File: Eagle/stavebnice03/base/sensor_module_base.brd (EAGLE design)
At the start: 21 x 21 mm, 19 parts

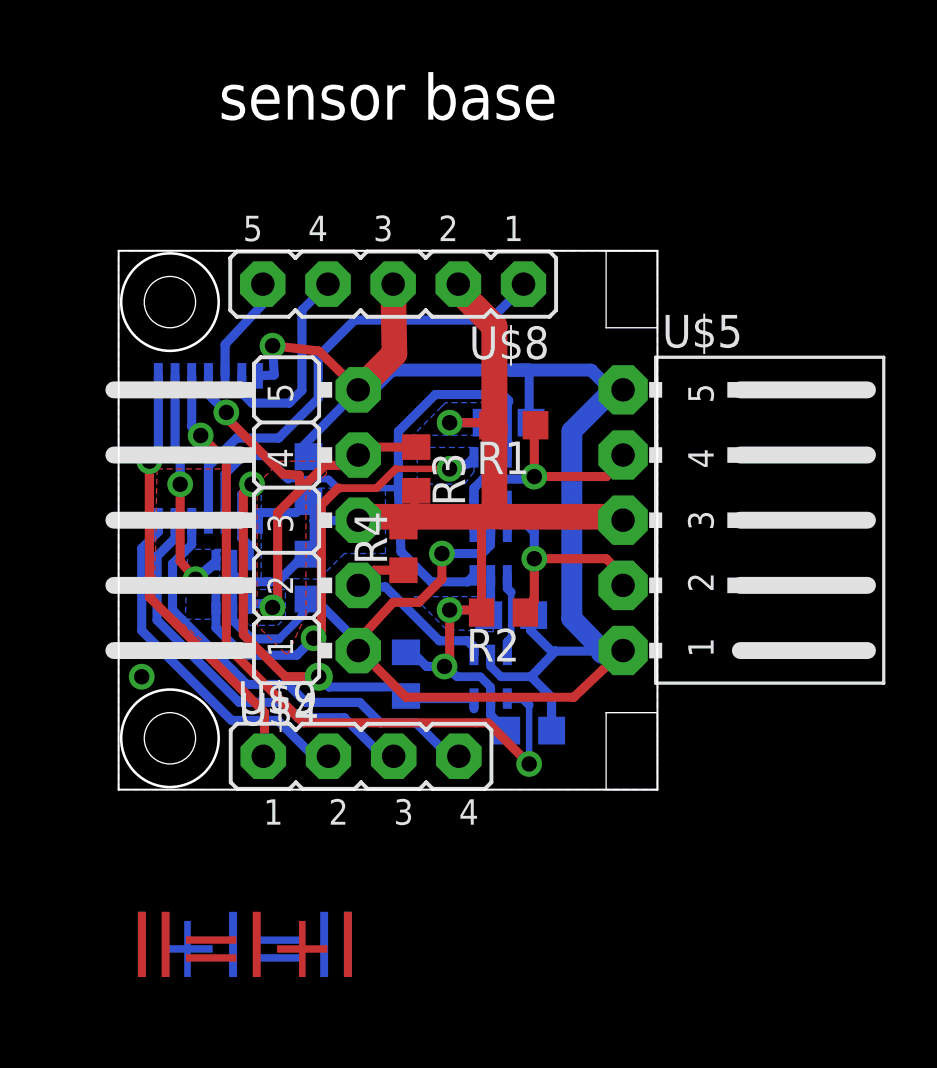
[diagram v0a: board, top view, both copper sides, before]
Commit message: layer coloring and place drawing moved to docu layer + changed sizes of names and values
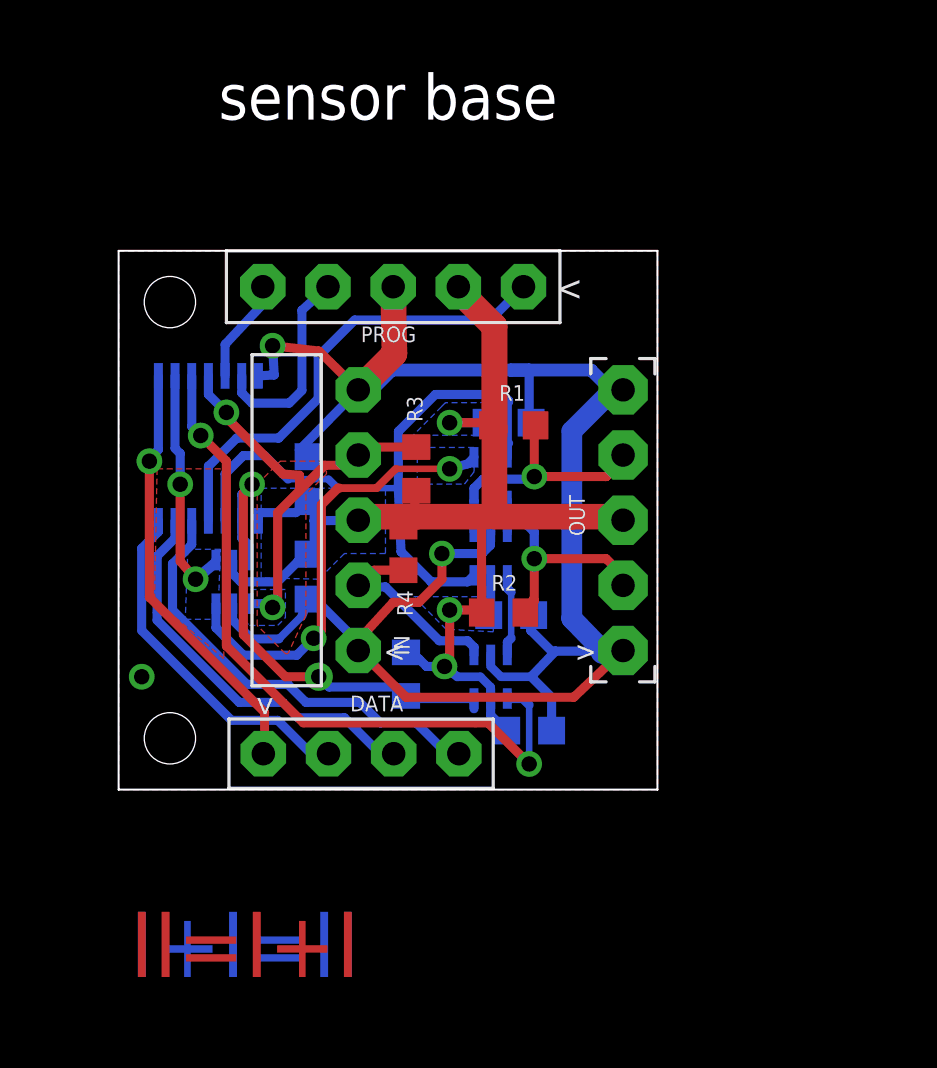
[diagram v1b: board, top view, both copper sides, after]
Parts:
- removed U$8: JUMPER5M, !stavebnice03:JUMPER5M
- removed U$9: JUMPER4M, !stavebnice03:JUMPER4M
- added DATA: JUMPER4M, !stavebnice03:JUMPER4M
- added PROG: JUMPER5M, !stavebnice03:JUMPER5M
- renumbered U$1 to U1, U$2 to U2, U$3 to U3, U$4 to IN, U$5 to OUT, U$6 to U4, U$7 to U5
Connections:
- net GND: now also PROG.3; no longer U$8.3
- net N$12: now also DATA.4; no longer U$9.4
- net N$13: now also PROG.1; no longer U$8.1
- net N$14: now also PROG.4; no longer U$8.4
- net N$15: now also PROG.5; no longer U$8.5
- net N$17: now also DATA.3; no longer U$9.3
- net N$18: now also DATA.1; no longer U$9.1
- net N$3: now also DATA.2; no longer U$9.2
- net VCC: now also PROG.2; no longer U$8.2
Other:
- outline, holes or cut-outs redrawn

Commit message: eagle adjustment for the Jíťa version
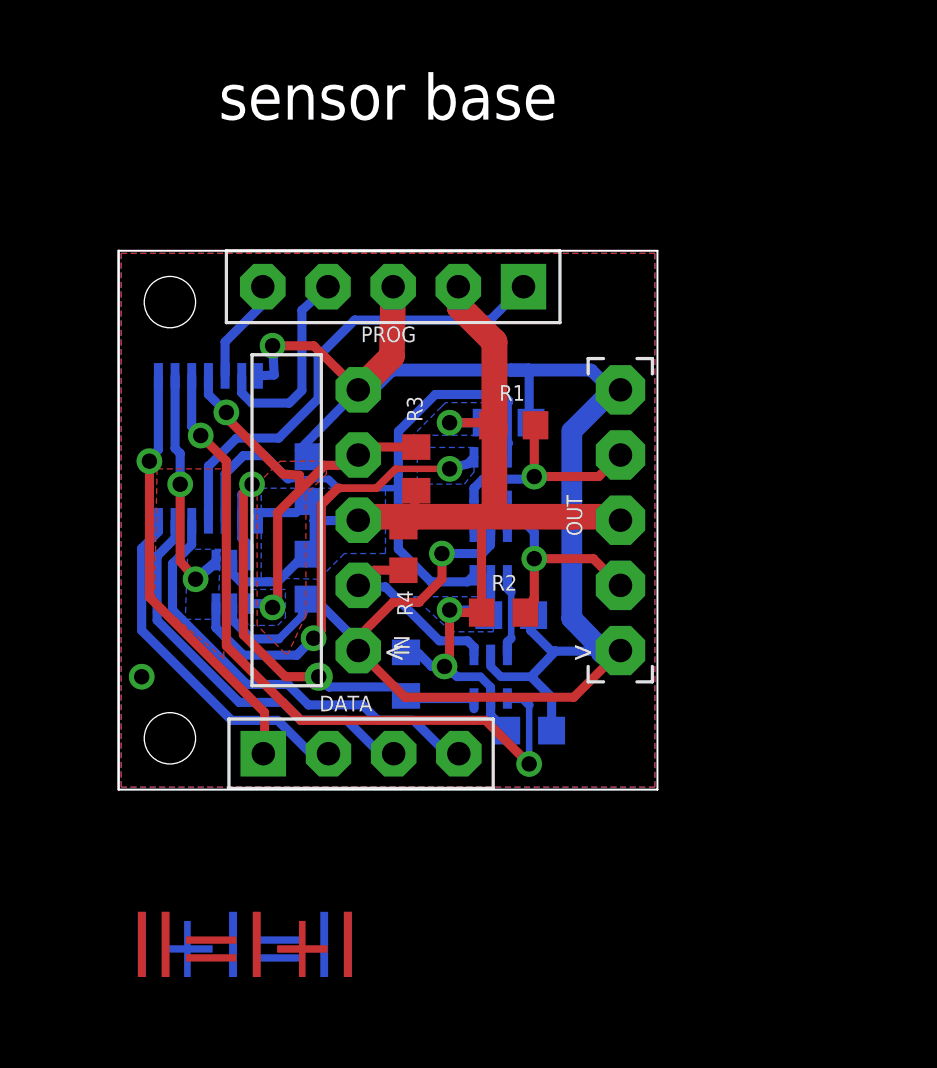
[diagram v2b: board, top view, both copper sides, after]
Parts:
- IN: value JUMPER5M-90 -> (none)
- OUT: value JUMPER5F-90 -> (none)
- U1: value 16F103-TSSOP -> 16F103
- U2, U3, U4, U5: value NC7SB3157P6X -> (none)
- moved OUT 0.10 mm to (22.1, 10.5)
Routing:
- net VCC: track 54.2 -> 55.7 mm
- net N$10: track 11.0 -> 10.2 mm
- net GND: track 78.7 -> 78.0 mm
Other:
- board text added: "GND"
- board text added: "RA0"
- board text added: "RA1"
- board text added: "RA3"
- board text added: "RC2"
- board text added: "RC3"
- board text added: "RC4"
- board text added: "RC5"
- board text added: "VCC"
- board text removed: "ma-na-bu"

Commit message: changes for pcb making by a seed studio
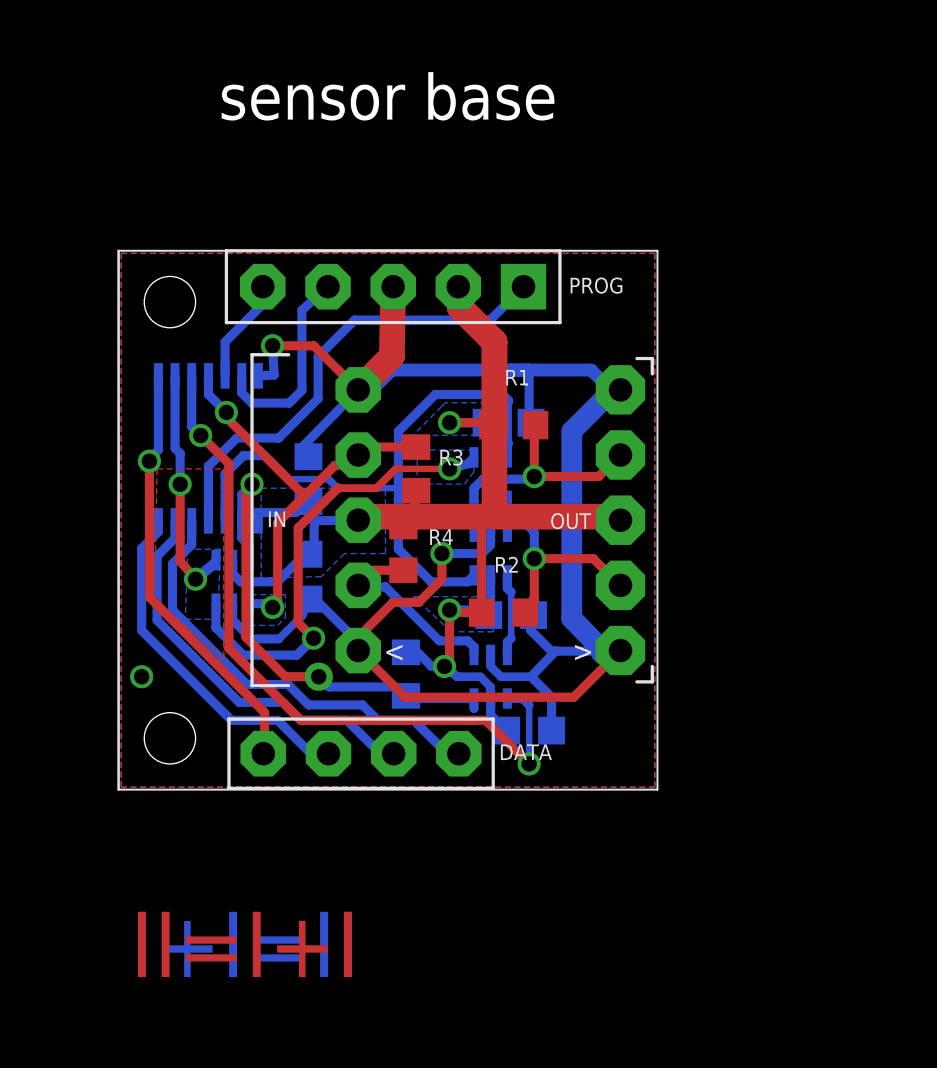
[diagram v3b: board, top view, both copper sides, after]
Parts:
- C1, C2, C3, C4, C5: value 100nF -> 100n
- IN: value (none) -> JUMPER5M-90
- OUT: value (none) -> JUMPER5F-90
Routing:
- removed copper zone on layer 1, net N$11
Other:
- board outline removed
- board text added: "kubo v0.1"
